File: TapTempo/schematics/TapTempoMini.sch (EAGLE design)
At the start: 55 parts, among them IC3 TL072D, Q2 8MHz, Q301 BC846, Q701 BC846, U1 STM32F100CBT6B, U3 NCP702

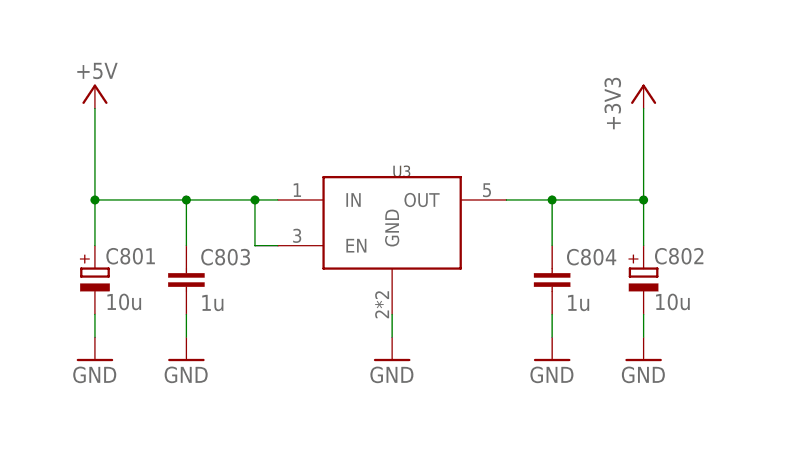
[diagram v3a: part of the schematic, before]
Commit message: moved and resized labels
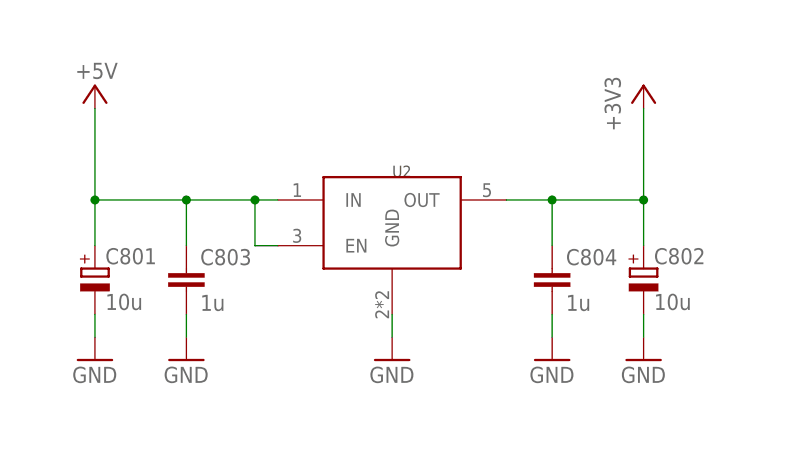
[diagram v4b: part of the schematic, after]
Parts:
- renumbered U3 to U2
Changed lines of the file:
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@@
 <part name="JP2" library="SparkFun" deviceset="M02" device="PTH"/>
 <part name="JP3" library="SparkFun" deviceset="M02" device="PTH"/>
-<part name="U3" library="Rebel" deviceset="NCP702" device=""/>
+<part name="U2" library="Rebel" deviceset="NCP702" device=""/>
 <part name="C803" library="resistor" deviceset="C-EU" device="C0603" value="1u"/>
 <part name="GND3" library="supply1" deviceset="GND" device=""/>
@@
 <instance part="JP2" gate="G$1" x="76.2" y="25.4" rot="R180"/>
 <instance part="JP3" gate="G$1" x="200.66" y="81.28" rot="R180"/>
-<instance part="U3" gate="G$1" x="162.56" y="162.56"/>
+<instance part="U2" gate="G$1" x="162.56" y="162.56"/>
 <instance part="C803" gate="G$1" x="139.7" y="157.48"/>
 <instance part="GND3" gate="1" x="139.7" y="147.32"/>
@@
 <pinref part="GND19" gate="1" pin="GND"/>
 <wire x1="162.56" y1="149.86" x2="162.56" y2="152.4" width="0.1524" layer="91"/>
-<pinref part="U3" gate="G$1" pin="GND"/>
+<pinref part="U2" gate="G$1" pin="GND"/>
 </segment>
 <segment>
@@
 <wire x1="129.54" y1="160.02" x2="129.54" y2="165.1" width="0.1524" layer="91"/>
 <junction x="129.54" y="165.1"/>
-<pinref part="U3" gate="G$1" pin="IN"/>
-<pinref part="U3" gate="G$1" pin="EN"/>
+<pinref part="U2" gate="G$1" pin="IN"/>
+<pinref part="U2" gate="G$1" pin="EN"/>
 <wire x1="149.86" y1="160.02" x2="147.32" y2="160.02" width="0.1524" layer="91"/>
 <wire x1="147.32" y1="160.02" x2="147.32" y2="165.1" width="0.1524" layer="91"/>
@@
 <wire x1="190.5" y1="165.1" x2="190.5" y2="160.02" width="0.1524" layer="91"/>
 <junction x="190.5" y="165.1"/>
-<pinref part="U3" gate="G$1" pin="OUT"/>
+<pinref part="U2" gate="G$1" pin="OUT"/>
 <pinref part="C804" gate="G$1" pin="1"/>
 <wire x1="180.34" y1="160.02" x2="180.34" y2="165.1" width="0.1524" layer="91"/>

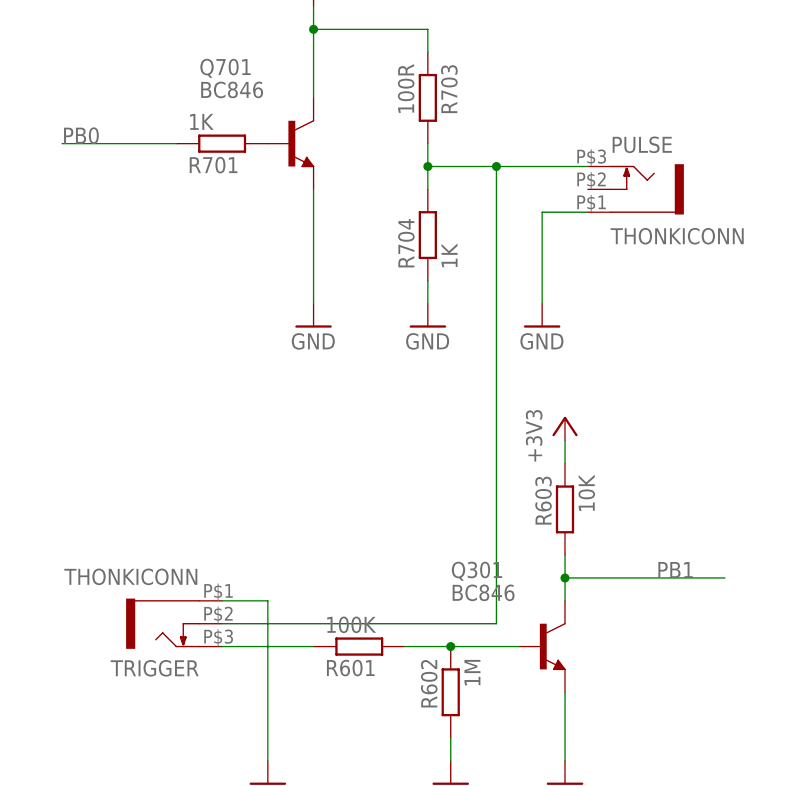
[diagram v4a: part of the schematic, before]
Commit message: added holes under jacks, rerouted to avoid jacks, and returned the normal connection to trigger input
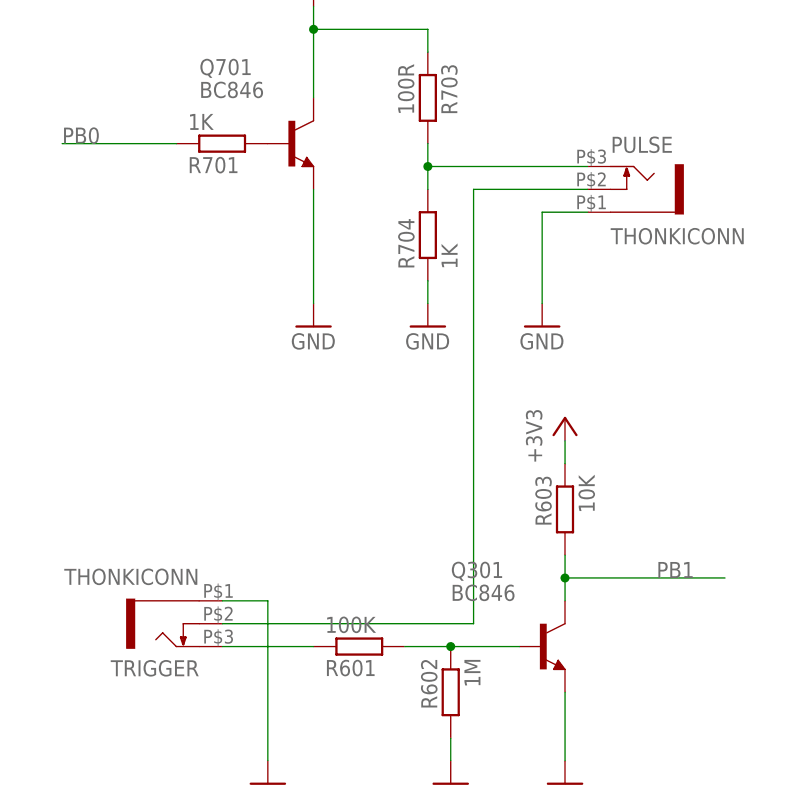
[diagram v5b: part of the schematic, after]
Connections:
- removed net N$35: PULSE.3, R703.2, R704.2, TRIGGER.4
- new net N$4: PULSE.3, R703.2, R704.2
- new net N$5: PULSE.4, TRIGGER.4
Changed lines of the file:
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@@
-</segment>
-</net>
-<net name="N$35" class="0">
-<segment>
-<pinref part="R704" gate="G$1" pin="2"/>
-<pinref part="R703" gate="G$1" pin="2"/>
-<wire x1="0" y1="152.4" x2="0" y2="149.86" width="0.1524" layer="91"/>
-<wire x1="0" y1="149.86" x2="0" y2="147.32" width="0.1524" layer="91"/>
-<wire x1="0" y1="149.86" x2="7.62" y2="149.86" width="0.1524" layer="91"/>
-<junction x="0" y="149.86"/>
-<pinref part="PULSE" gate="G$1" pin="3"/>
-<pinref part="TRIGGER" gate="G$1" pin="4"/>
-<wire x1="7.62" y1="149.86" x2="17.78" y2="149.86" width="0.1524" layer="91"/>
-<wire x1="-22.86" y1="99.06" x2="7.62" y2="99.06" width="0.1524" layer="91"/>
-<wire x1="7.62" y1="99.06" x2="7.62" y2="149.86" width="0.1524" layer="91"/>
-<junction x="7.62" y="149.86"/>
 </segment>
 </net>
@@
 </segment>
 </net>
+<net name="N$4" class="0">
+<segment>
+<pinref part="R704" gate="G$1" pin="2"/>
+<pinref part="PULSE" gate="G$1" pin="3"/>
+<pinref part="R703" gate="G$1" pin="2"/>
+<wire x1="0" y1="152.4" x2="0" y2="149.86" width="0.1524" layer="91"/>
+<junction x="0" y="149.86"/>
+<wire x1="0" y1="149.86" x2="17.78" y2="149.86" width="0.1524" layer="91"/>
+<wire x1="0" y1="149.86" x2="0" y2="147.32" width="0.1524" layer="91"/>
+</segment>
+</net>
+<net name="N$5" class="0">
+<segment>
+<pinref part="PULSE" gate="G$1" pin="4"/>
+<wire x1="17.78" y1="147.32" x2="5.08" y2="147.32" width="0.1524" layer="91"/>
+<wire x1="5.08" y1="147.32" x2="5.08" y2="99.06" width="0.1524" layer="91"/>
+<pinref part="TRIGGER" gate="G$1" pin="4"/>
+<wire x1="-22.86" y1="99.06" x2="5.08" y2="99.06" width="0.1524" layer="91"/>
+</segment>
+</net>

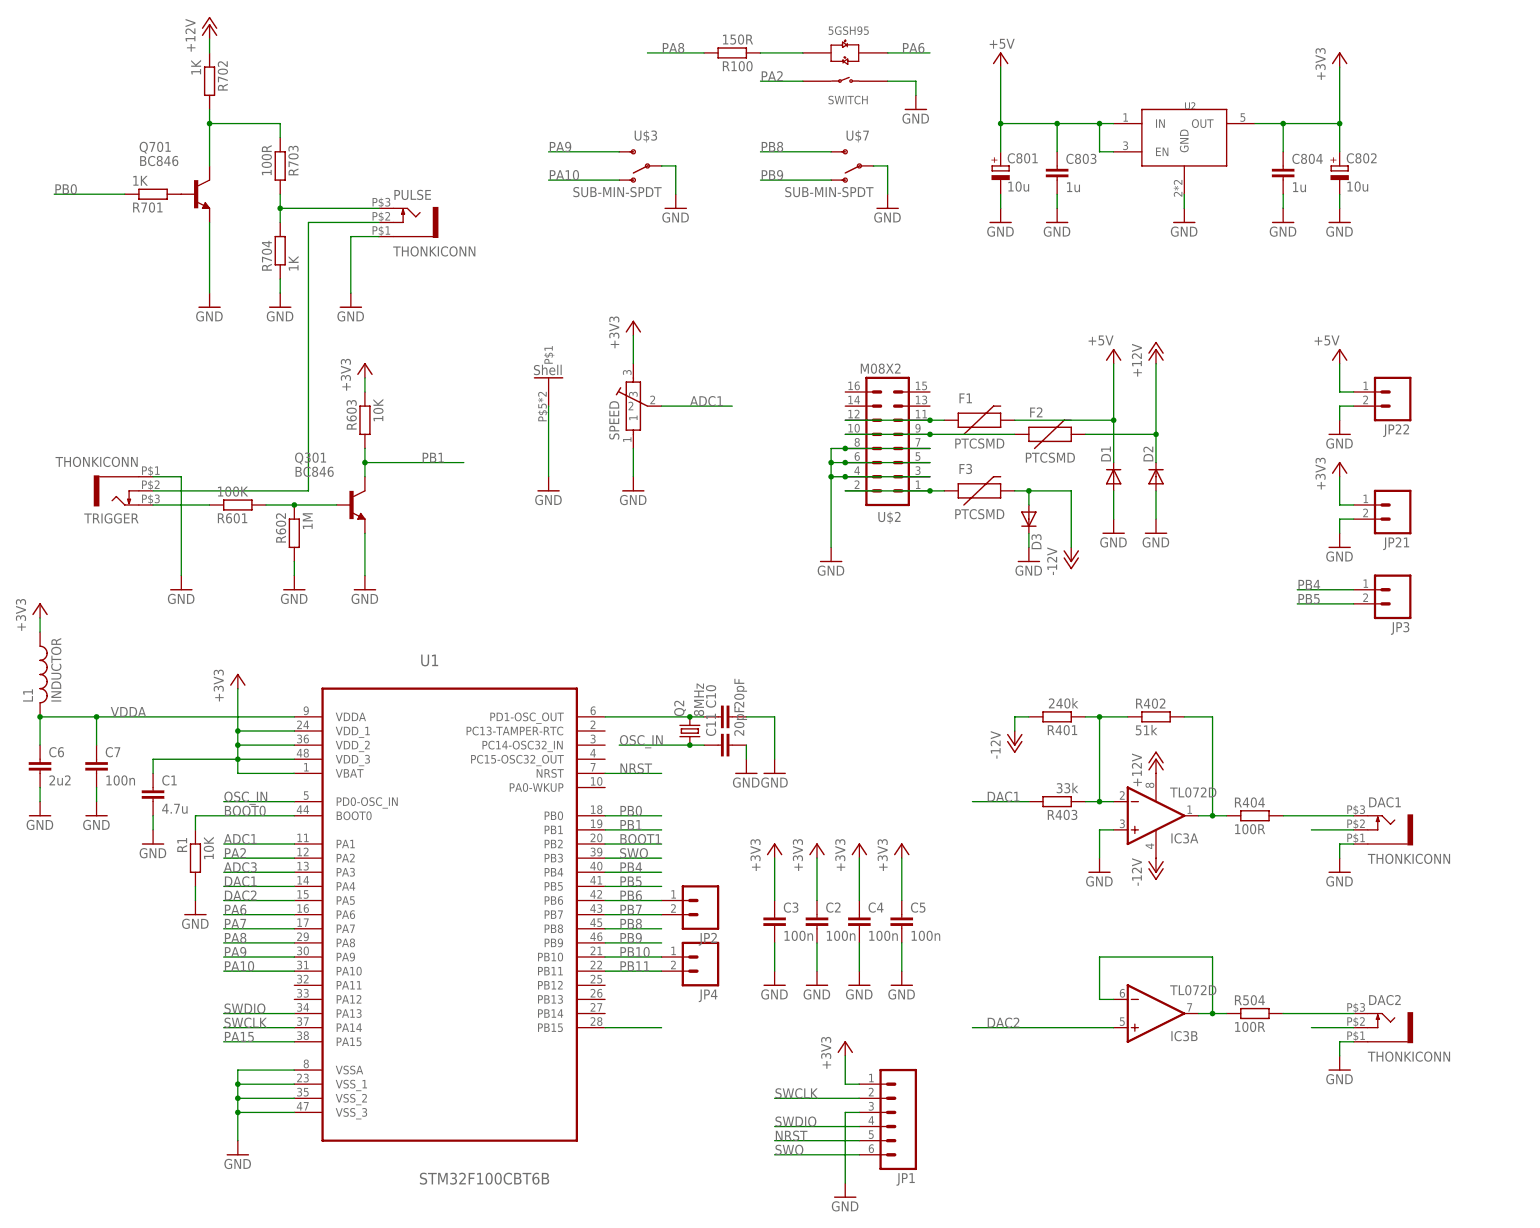
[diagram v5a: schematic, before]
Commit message: added gnd points for jumpers
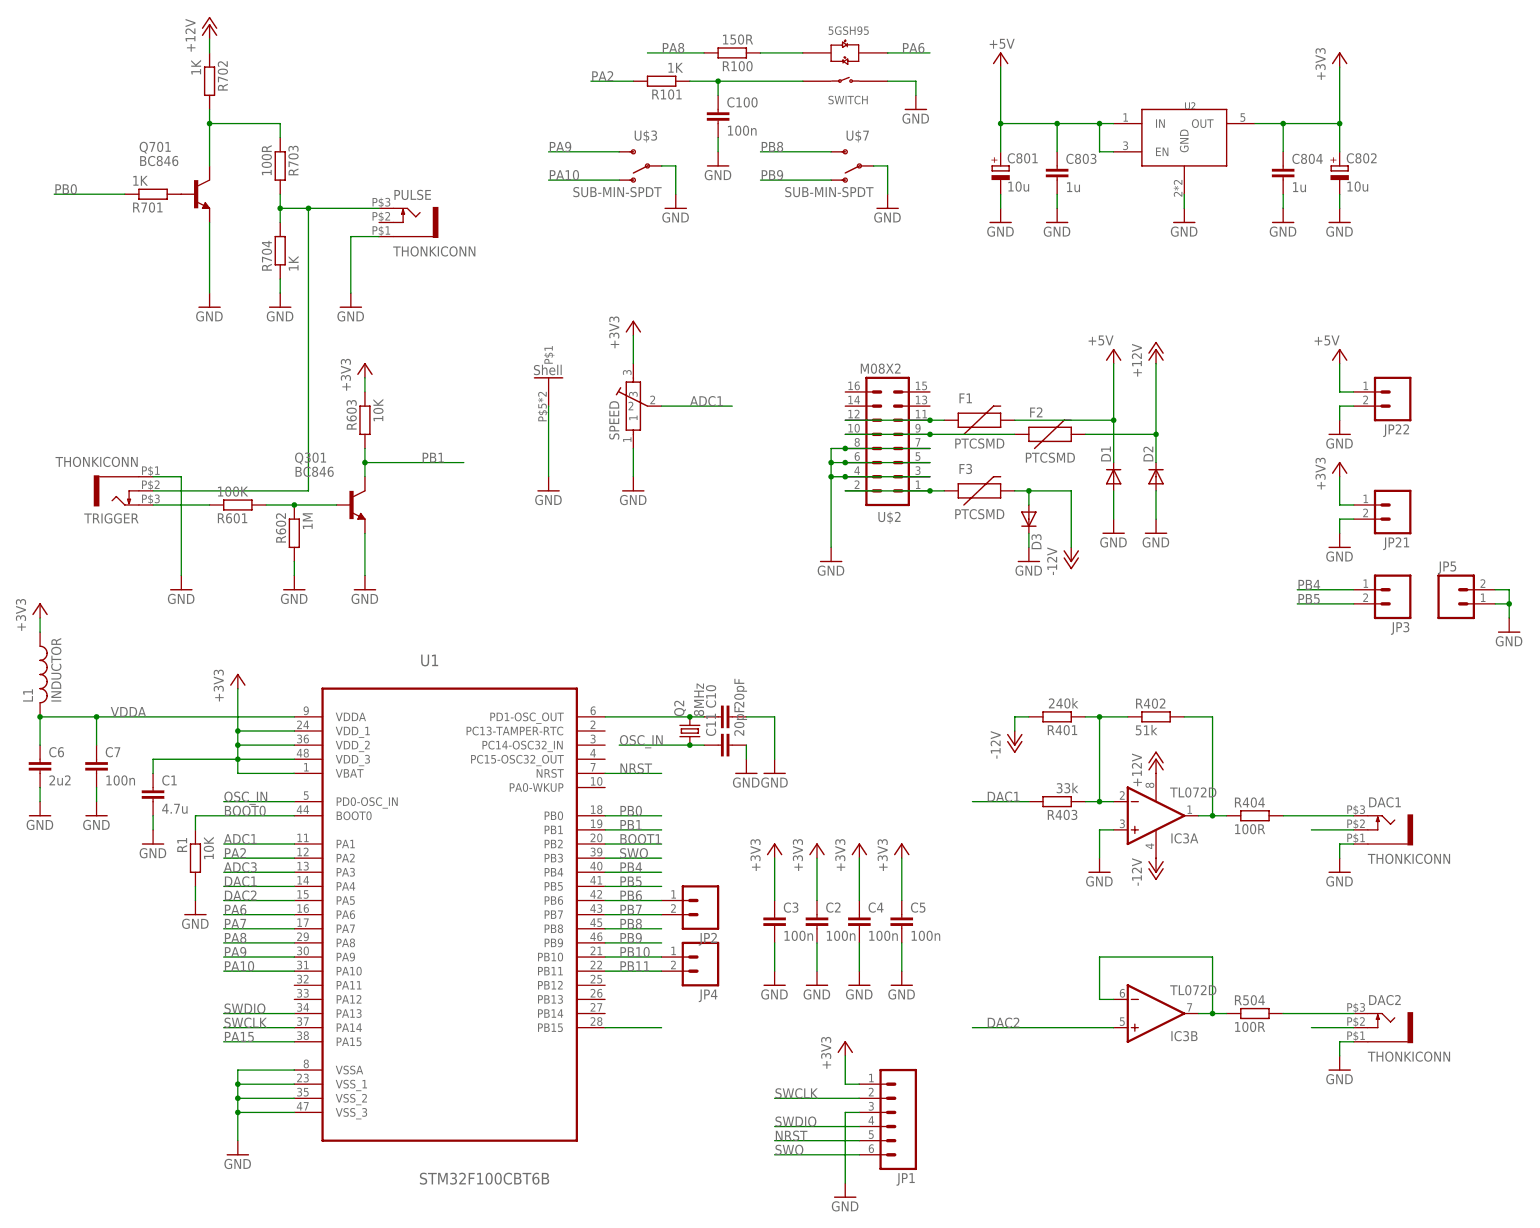
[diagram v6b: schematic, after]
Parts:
- added C100: 100n, resistor:C-EUC0603
- added JP5: (no value), SparkFun:M02PTH
- added R101: 1K, resistor:R-EU_R0603
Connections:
- removed net N$4: PULSE.3, R703.2, R704.2
- new net SWITCH_A: C100.1, R101.1, U$1.SWITCH_A
- net GND: now also C100.2, JP5.1, JP5.2
- net N$5: now also PULSE.3, R703.2, R704.2; no longer PULSE.4
- net PA2: now also R101.2; no longer U$1.SWITCH_A
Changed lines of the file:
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@@
 <part name="U$3" library="Rebel" deviceset="SUB-MIN-SPDT" device=""/>
 <part name="GND17" library="supply1" deviceset="GND" device=""/>
+<part name="R101" library="resistor" deviceset="R-EU_" device="R0603" value="1K"/>
+<part name="C100" library="resistor" deviceset="C-EU" device="C0603" value="100n"/>
+<part name="GND5" library="supply1" deviceset="GND" device=""/>
+<part name="JP5" library="SparkFun" deviceset="M02" device="PTH"/>
+<part name="GND18" library="supply1" deviceset="GND" device=""/>
 </parts>
 <sheets>
@@
 <instance part="U$3" gate="G$1" x="66.04" y="157.48" rot="R180"/>
 <instance part="GND17" gate="1" x="71.12" y="149.86"/>
+<instance part="R101" gate="G$1" x="68.58" y="172.72" rot="R180"/>
+<instance part="C100" gate="G$1" x="78.74" y="167.64"/>
+<instance part="GND5" gate="1" x="78.74" y="157.48"/>
+<instance part="JP5" gate="G$1" x="210.82" y="78.74"/>
+<instance part="GND18" gate="1" x="220.98" y="73.66"/>
 </instances>
 <busses>
@@
 <wire x1="71.12" y1="157.48" x2="71.12" y2="152.4" width="0.1524" layer="91"/>
 </segment>
+<segment>
+<pinref part="C100" gate="G$1" pin="2"/>
+<pinref part="GND5" gate="1" pin="GND"/>
+<wire x1="78.74" y1="160.02" x2="78.74" y2="162.56" width="0.1524" layer="91"/>
+</segment>
+<segment>
+<pinref part="JP5" gate="G$1" pin="1"/>
+<pinref part="GND18" gate="1" pin="GND"/>
+<wire x1="218.44" y1="78.74" x2="220.98" y2="78.74" width="0.1524" layer="91"/>
+<wire x1="220.98" y1="78.74" x2="220.98" y2="76.2" width="0.1524" layer="91"/>
+<pinref part="JP5" gate="G$1" pin="2"/>
+<wire x1="218.44" y1="81.28" x2="220.98" y2="81.28" width="0.1524" layer="91"/>
+<wire x1="220.98" y1="81.28" x2="220.98" y2="78.74" width="0.1524" layer="91"/>
+<junction x="220.98" y="78.74"/>
+</segment>
 </net>
 <net name="-12V" class="0">
@@
 </segment>
 <segment>
-<pinref part="U$1" gate="G$1" pin="SWITCH_A"/>
-<wire x1="93.98" y1="172.72" x2="86.36" y2="172.72" width="0.1524" layer="91"/>
-<label x="86.36" y="172.72" size="1.778" layer="95"/>
+<pinref part="R101" gate="G$1" pin="2"/>
+<wire x1="63.5" y1="172.72" x2="55.88" y2="172.72" width="0.1524" layer="91"/>
+<label x="55.88" y="172.72" size="1.778" layer="95"/>
 </segment>
 </net>
@@
 </segment>
 </net>
-<net name="N$4" class="0">
-<segment>
+<net name="N$5" class="0">
+<segment>
+<wire x1="5.08" y1="149.86" x2="5.08" y2="99.06" width="0.1524" layer="91"/>
+<pinref part="TRIGGER" gate="G$1" pin="4"/>
+<wire x1="-22.86" y1="99.06" x2="5.08" y2="99.06" width="0.1524" layer="91"/>
 <pinref part="R704" gate="G$1" pin="2"/>
 <pinref part="PULSE" gate="G$1" pin="3"/>
@@
 <wire x1="0" y1="152.4" x2="0" y2="149.86" width="0.1524" layer="91"/>
 <junction x="0" y="149.86"/>
-<wire x1="0" y1="149.86" x2="17.78" y2="149.86" width="0.1524" layer="91"/>
+<wire x1="0" y1="149.86" x2="5.08" y2="149.86" width="0.1524" layer="91"/>
+<wire x1="5.08" y1="149.86" x2="17.78" y2="149.86" width="0.1524" layer="91"/>
 <wire x1="0" y1="149.86" x2="0" y2="147.32" width="0.1524" layer="91"/>
-</segment>
-</net>
-<net name="N$5" class="0">
-<segment>
-<pinref part="PULSE" gate="G$1" pin="4"/>
-<wire x1="17.78" y1="147.32" x2="5.08" y2="147.32" width="0.1524" layer="91"/>
-<wire x1="5.08" y1="147.32" x2="5.08" y2="99.06" width="0.1524" layer="91"/>
-<pinref part="TRIGGER" gate="G$1" pin="4"/>
-<wire x1="-22.86" y1="99.06" x2="5.08" y2="99.06" width="0.1524" layer="91"/>
-</segment>
-</net>
+<junction x="5.08" y="149.86"/>
+</segment>
+</net>
+<net name="SWITCH_A" class="0">
+<segment>
+<pinref part="R101" gate="G$1" pin="1"/>
+<pinref part="C100" gate="G$1" pin="1"/>
+<wire x1="73.66" y1="172.72" x2="78.74" y2="172.72" width="0.1524" layer="91"/>
+<wire x1="78.74" y1="172.72" x2="78.74" y2="170.18" width="0.1524" layer="91"/>
+<pinref part="U$1" gate="G$1" pin="SWITCH_A"/>
+<wire x1="93.98" y1="172.72" x2="78.74" y2="172.72" width="0.1524" layer="91"/>
+<junction x="78.74" y="172.72"/>
+</segment>
+</net>
